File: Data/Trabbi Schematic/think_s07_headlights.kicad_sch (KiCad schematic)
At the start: 12 parts, among them K1 DRL Relay R5, K2 Park Light Relay R17, SW1 Headlight Switch (C25)

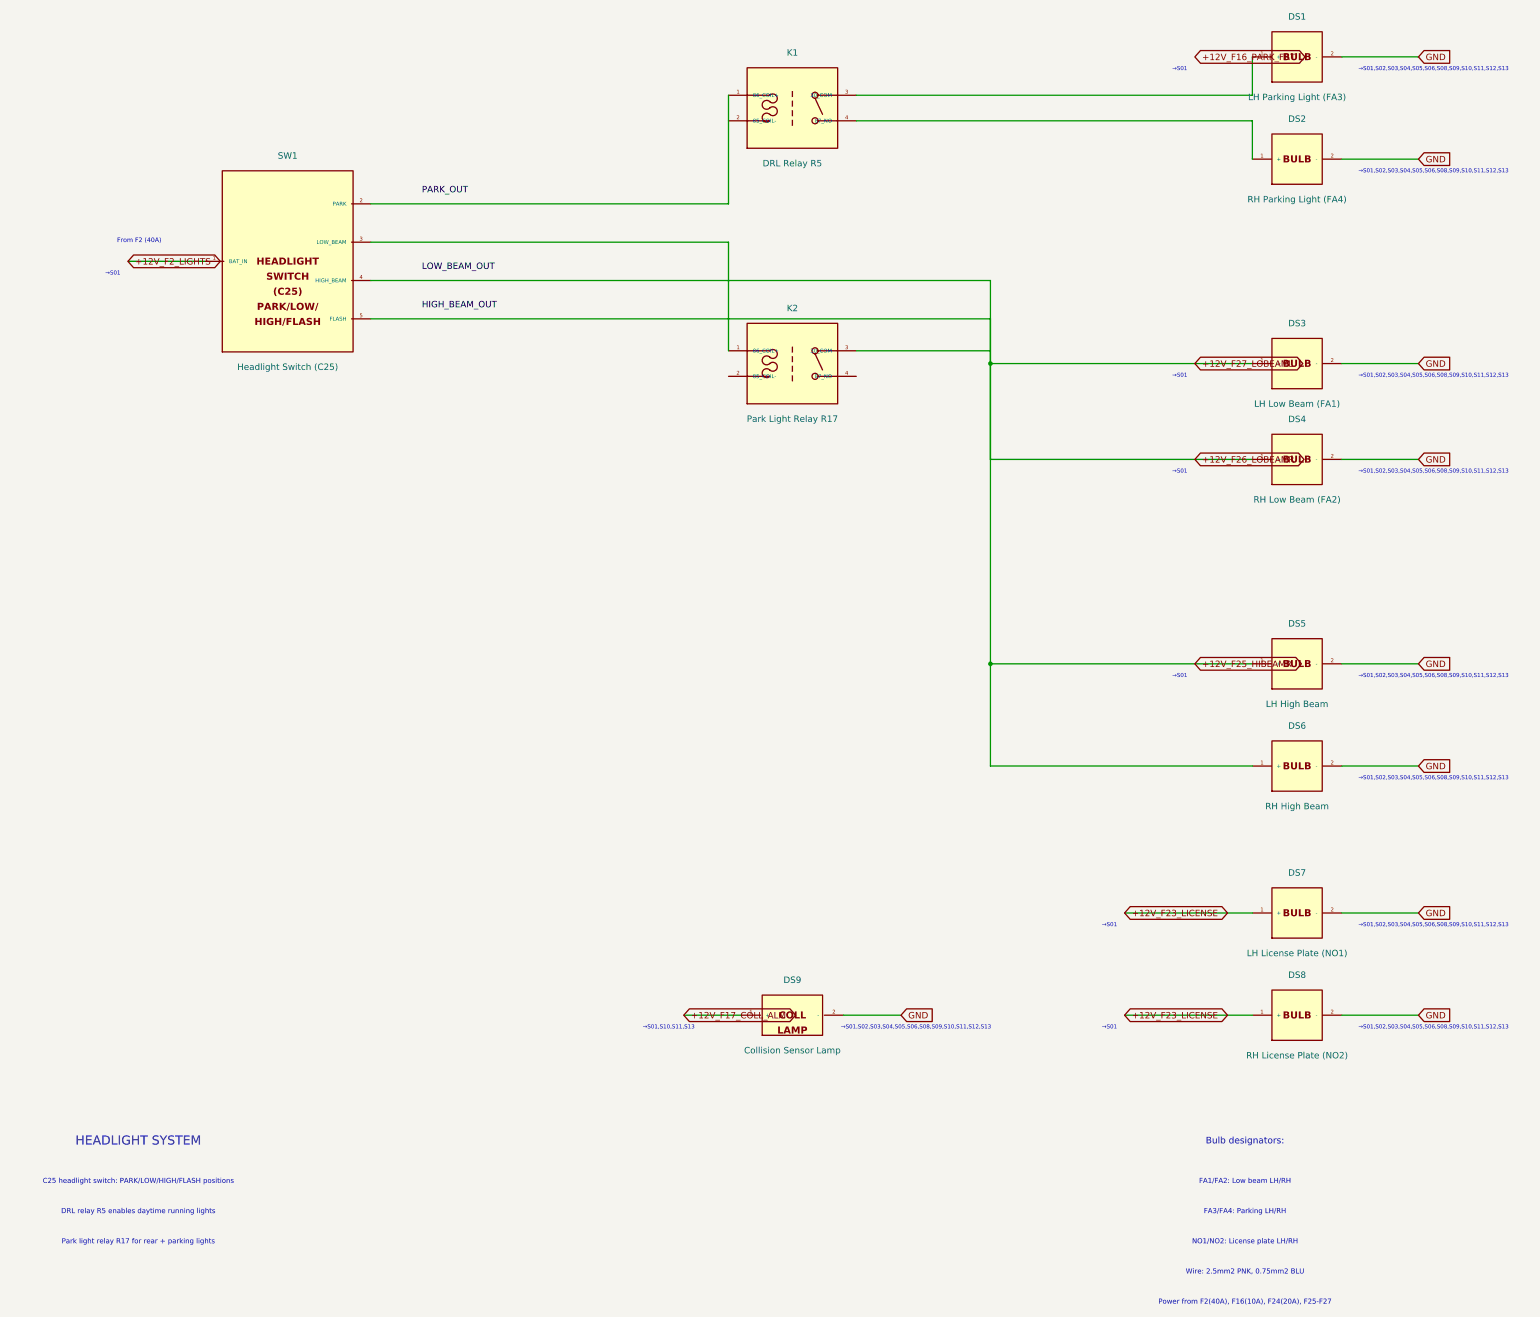
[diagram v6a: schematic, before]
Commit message: Relay symbol for flasher, label justify set to auto
- Flasher Relay (Think:FLASHER_RELAY) now has coil+switch graphics
  matching the standard relay symbol style
- All relays (SPST, SPDT, Flasher) use consistent coil+switch body
- Remove (justify left) from all label and global_label effects —
  KiCad 9 auto-determines text alignment based on label orientation

Co-Authored-By: Claude Opus 4.6 <noreply@anthropic.com>
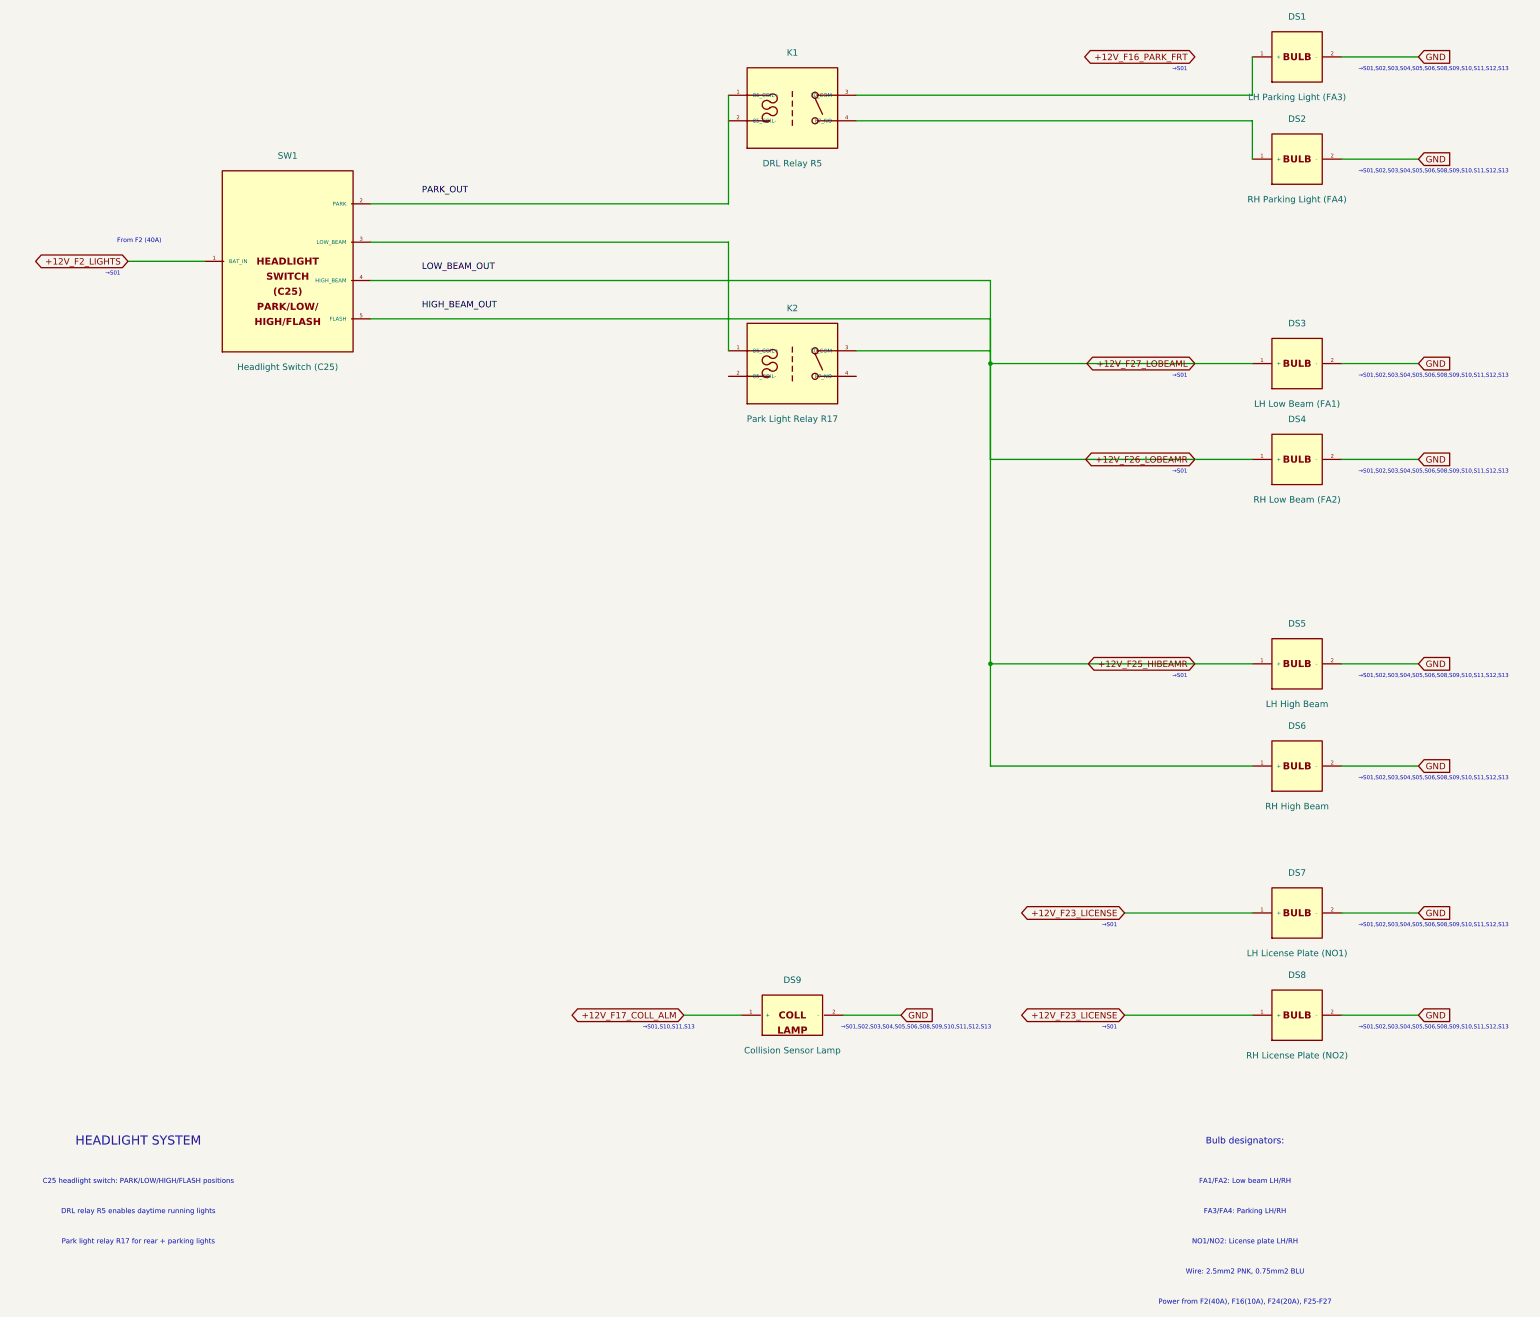
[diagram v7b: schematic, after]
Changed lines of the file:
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@@
   )
   (global_label "+12V_F2_LIGHTS" (shape bidirectional) (at 27.940 80.010 180)
-    (effects (font (size 1.27 1.27)) (justify left))
+    (effects (font (size 1.27 1.27)))
     (property "Intersheetrefs" "${INTERSHEET_REFS}" (at 27.940 80.010 0)
       (effects (font (size 1.27 1.27)) hide)
@@
   )
   (label "PARK_OUT" (at 86.360 66.040 0)
-    (effects (font (size 1.27 1.27)) (justify left))
+    (effects (font (size 1.27 1.27)))
   )
   (wire (pts (xy 76.200 76.200) (xy 147.320 76.200))
@@
   )
   (label "LOW_BEAM_OUT" (at 86.360 81.280 0)
-    (effects (font (size 1.27 1.27)) (justify left))
+    (effects (font (size 1.27 1.27)))
   )
   (wire (pts (xy 76.200 91.440) (xy 199.390 91.440))
@@
   )
   (label "HIGH_BEAM_OUT" (at 86.360 88.900 0)
-    (effects (font (size 1.27 1.27)) (justify left))
+    (effects (font (size 1.27 1.27)))
   )
   (wire (pts (xy 172.720 46.990) (xy 251.460 46.990))
@@
   )
   (global_label "GND" (shape input) (at 284.480 39.370 0)
-    (effects (font (size 1.27 1.27)) (justify left))
+    (effects (font (size 1.27 1.27)))
     (property "Intersheetrefs" "${INTERSHEET_REFS}" (at 284.480 39.370 0)
       (effects (font (size 1.27 1.27)) hide)
@@
   )
   (global_label "GND" (shape input) (at 284.480 59.690 0)
-    (effects (font (size 1.27 1.27)) (justify left))
+    (effects (font (size 1.27 1.27)))
     (property "Intersheetrefs" "${INTERSHEET_REFS}" (at 284.480 59.690 0)
       (effects (font (size 1.27 1.27)) hide)
@@
   )
   (global_label "GND" (shape input) (at 284.480 100.330 0)
-    (effects (font (size 1.27 1.27)) (justify left))
+    (effects (font (size 1.27 1.27)))
     (property "Intersheetrefs" "${INTERSHEET_REFS}" (at 284.480 100.330 0)
       (effects (font (size 1.27 1.27)) hide)
@@
   )
   (global_label "GND" (shape input) (at 284.480 119.380 0)
-    (effects (font (size 1.27 1.27)) (justify left))
+    (effects (font (size 1.27 1.27)))
     (property "Intersheetrefs" "${INTERSHEET_REFS}" (at 284.480 119.380 0)
       (effects (font (size 1.27 1.27)) hide)
@@
   )
   (global_label "GND" (shape input) (at 284.480 160.020 0)
-    (effects (font (size 1.27 1.27)) (justify left))
+    (effects (font (size 1.27 1.27)))
     (property "Intersheetrefs" "${INTERSHEET_REFS}" (at 284.480 160.020 0)
       (effects (font (size 1.27 1.27)) hide)
@@
   )
   (global_label "GND" (shape input) (at 284.480 180.340 0)
-    (effects (font (size 1.27 1.27)) (justify left))
+    (effects (font (size 1.27 1.27)))
     (property "Intersheetrefs" "${INTERSHEET_REFS}" (at 284.480 180.340 0)
       (effects (font (size 1.27 1.27)) hide)
@@
   )
   (global_label "GND" (shape input) (at 284.480 209.550 0)
-    (effects (font (size 1.27 1.27)) (justify left))
+    (effects (font (size 1.27 1.27)))
     (property "Intersheetrefs" "${INTERSHEET_REFS}" (at 284.480 209.550 0)
       (effects (font (size 1.27 1.27)) hide)
@@
   )
   (global_label "GND" (shape input) (at 284.480 229.870 0)
-    (effects (font (size 1.27 1.27)) (justify left))
+    (effects (font (size 1.27 1.27)))
     (property "Intersheetrefs" "${INTERSHEET_REFS}" (at 284.480 229.870 0)
       (effects (font (size 1.27 1.27)) hide)
@@
   )
   (global_label "+12V_F23_LICENSE" (shape bidirectional) (at 226.060 209.550 180)
-    (effects (font (size 1.27 1.27)) (justify left))
+    (effects (font (size 1.27 1.27)))
     (property "Intersheetrefs" "${INTERSHEET_REFS}" (at 226.060 209.550 0)
       (effects (font (size 1.27 1.27)) hide)
@@
   )
   (global_label "+12V_F23_LICENSE" (shape bidirectional) (at 226.060 229.870 180)
-    (effects (font (size 1.27 1.27)) (justify left))
+    (effects (font (size 1.27 1.27)))
     (property "Intersheetrefs" "${INTERSHEET_REFS}" (at 226.060 229.870 0)
       (effects (font (size 1.27 1.27)) hide)
@@
   )
   (global_label "+12V_F16_PARK_FRT" (shape bidirectional) (at 240.030 39.370 180)
-    (effects (font (size 1.27 1.27)) (justify left))
+    (effects (font (size 1.27 1.27)))
     (property "Intersheetrefs" "${INTERSHEET_REFS}" (at 240.030 39.370 0)
       (effects (font (size 1.27 1.27)) hide)
@@
   )
   (global_label "+12V_F27_LOBEAML" (shape bidirectional) (at 240.030 100.330 180)
-    (effects (font (size 1.27 1.27)) (justify left))
+    (effects (font (size 1.27 1.27)))
     (property "Intersheetrefs" "${INTERSHEET_REFS}" (at 240.030 100.330 0)
       (effects (font (size 1.27 1.27)) hide)
@@
   )
   (global_label "+12V_F26_LOBEAMR" (shape bidirectional) (at 240.030 119.380 180)
-    (effects (font (size 1.27 1.27)) (justify left))
+    (effects (font (size 1.27 1.27)))
     (property "Intersheetrefs" "${INTERSHEET_REFS}" (at 240.030 119.380 0)
       (effects (font (size 1.27 1.27)) hide)
@@
   )
   (global_label "+12V_F25_HIBEAMR" (shape bidirectional) (at 240.030 160.020 180)
-    (effects (font (size 1.27 1.27)) (justify left))
+    (effects (font (size 1.27 1.27)))
     (property "Intersheetrefs" "${INTERSHEET_REFS}" (at 240.030 160.020 0)
       (effects (font (size 1.27 1.27)) hide)
@@
   )
   (global_label "+12V_F17_COLL_ALM" (shape bidirectional) (at 138.430 229.870 180)
-    (effects (font (size 1.27 1.27)) (justify left))
+    (effects (font (size 1.27 1.27)))
     (property "Intersheetrefs" "${INTERSHEET_REFS}" (at 138.430 229.870 0)
       (effects (font (size 1.27 1.27)) hide)
@@
   )
   (global_label "GND" (shape input) (at 181.610 229.870 0)
-    (effects (font (size 1.27 1.27)) (justify left))
+    (effects (font (size 1.27 1.27)))
     (property "Intersheetrefs" "${INTERSHEET_REFS}" (at 181.610 229.870 0)
       (effects (font (size 1.27 1.27)) hide)
